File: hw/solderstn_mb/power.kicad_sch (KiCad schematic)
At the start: 74 parts, among them J301 Conn_WR-FAST_01x04, J302 Molex_MicroFit_30-43045-0421, J303 Conn_WR-FAST_01x02, Q301 Si4497DY, Q302 Si4497DY, Q303 DMG1012T, U301 TPS54332DDA, U302 TLV1117LV30DCY, U303 TLV1117LV30DCY, U304 TLV1117LV30DCY, U305 AP22811AW5

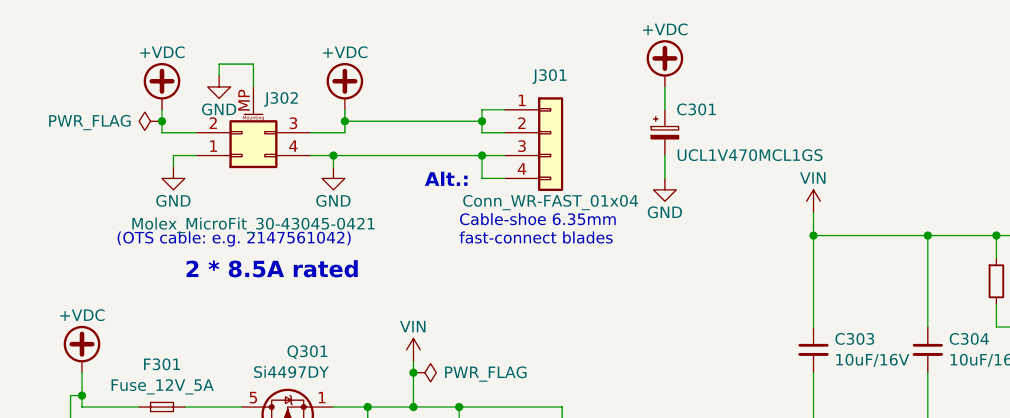
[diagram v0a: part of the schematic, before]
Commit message: Placeholder 3d-models for rear-panel (w. conns), PSU, Bottom-plate, front-panel (w. conns), outer fp
With these placeholder mech. objects, the build-in 3d view of MB pcb features most of the mechanical
objects that constrain components placements. So 3d-view can be used to quickly check and iterate
placements to avoid 3d collisions, without having to first export MB STEP into FreeCAD and muck around
only to have to repeat again for each iteration
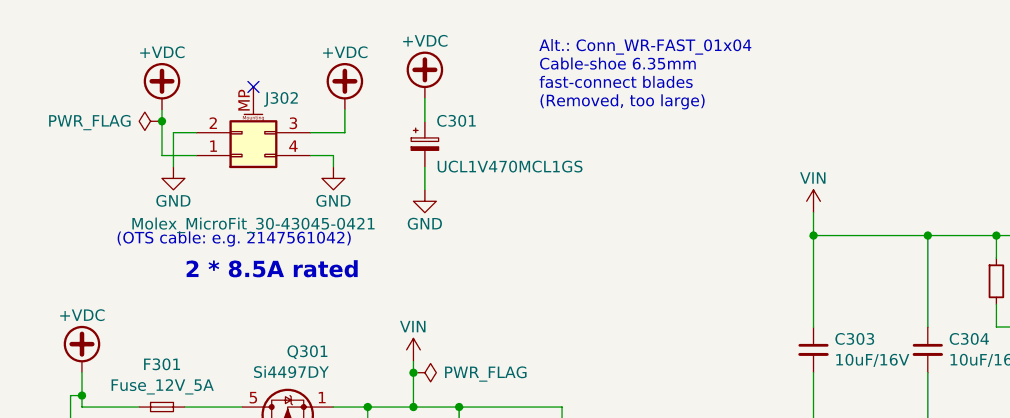
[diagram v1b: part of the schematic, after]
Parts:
- removed J301: Conn_WR-FAST_01x04, customlib_mj_fp:WR-FAST_508_4_V, symbol customlib_mj:Conn_WR-FAST_01x04
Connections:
- net +VDC: now also J302.1 (Pin_1); no longer J302.2 (Pin_2)
- net GND: now also J302.2 (Pin_2); no longer J302.1 (Pin_1), J302.MP (MountPin)
- no-connect marks 0 -> 1
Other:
- note added: "Alt.: Conn_WR-FAST_01x04 Cable-shoe 6.35mm fast-connect blades (Removed, too large)"
- note removed: "Alt.:"
- note removed: "Cable-shoe 6.35mm fast-connect blades"
- moved on the sheet: C301

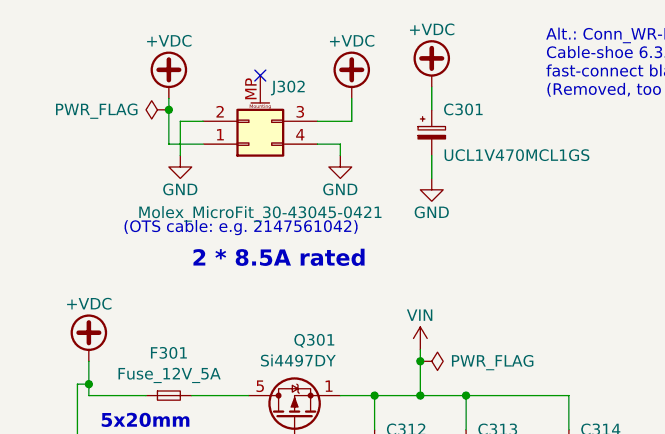
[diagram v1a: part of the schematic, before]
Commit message: solderstn_mb::power - changed generic 2x2 connector to customlib_mj:Molex_MicroFit 2x2
(and a whole bunch of other automatic changes, crap)
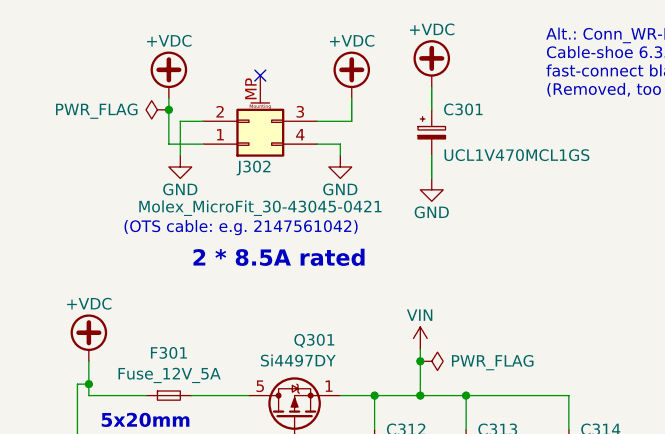
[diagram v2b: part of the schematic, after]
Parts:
- J302: symbol Connector_Generic_MountingPin:Conn_02x02_Counter_Clockwise_MountingPin -> customlib_mj:Molex_MicroFit_30-43045-0421
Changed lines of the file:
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@@
     (pin "1")
   )
-  (symbol (lib_id "Connector_Generic_MountingPin:Conn_02x02_Counter_Clockwise_MountingPin") (at 34.29 27.94 0) (mirror x) (unit 1)
+  (symbol (lib_id "customlib_mj:Molex_MicroFit_30-43045-0421") (at 34.29 27.94 0) (mirror x) (unit 1)
     (in_bom yes) (on_board yes)
-    (property "Reference" "J302" (id 0) (at 36.83 21.59 0)
+    (property "Reference" "J302" (id 0) (at 33.02 30.48 0)
       (effects (font (size 1.27 1.27)) (justify left))
     )
-    (property "Value" "Molex_MicroFit_30-43045-0421" (id 1) (at 35.56 35.56 0))
-    (property "Footprint" "customlib_mj_fp:Molex_Micro-Fit_3.0_43045-0421_2x02-1MP_P3.00mm_Horizontal" (id 2) (at 34.29 27.94 0)
+    (property "Value" "Molex_MicroFit_30-43045-0421" (id 1) (at 35.56 34.925 0))
+    (property "Footprint" "customlib_mj_fp:Molex_Micro-Fit_3.0_43045-0421_2x02-1MP_P3.00mm_Horizontal" (id 2) (at 34.29 17.78 0)
       (effects (font (size 1.27 1.27)) hide)
     )
-    (property "Datasheet" "https://www.molex.com/molex/products/part-detail/pcb_headers/0430450421" (id 3) (at 34.29 27.94 0)
+    (property "Datasheet" "https://www.molex.com/molex/products/part-detail/pcb_headers/0430450421" (id 3) (at 35.56 33.02 0)
       (effects (font (size 1.27 1.27)) hide)
     )

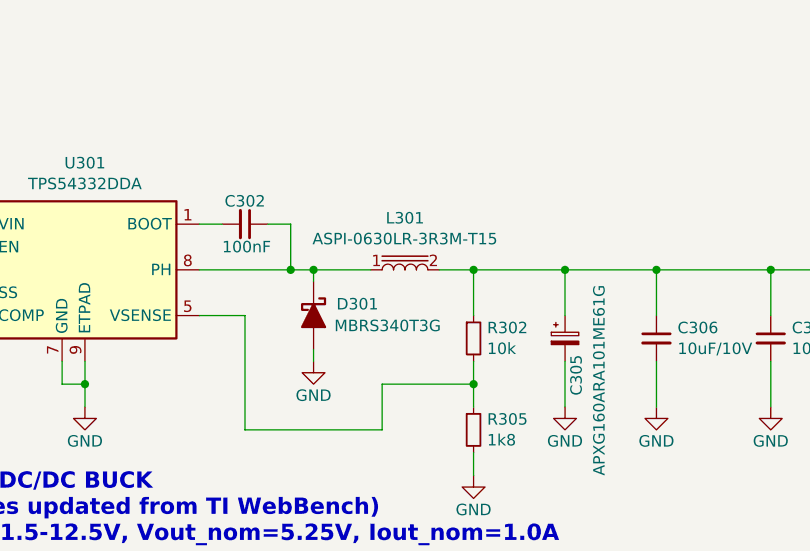
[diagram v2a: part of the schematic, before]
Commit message: hw: long-standing uncommitted stuff; mostly auto-updates (v7) fw: remove L052 tree (CMSIS & std-HAL shouldn't be committed and it was the wrong device name anyway)
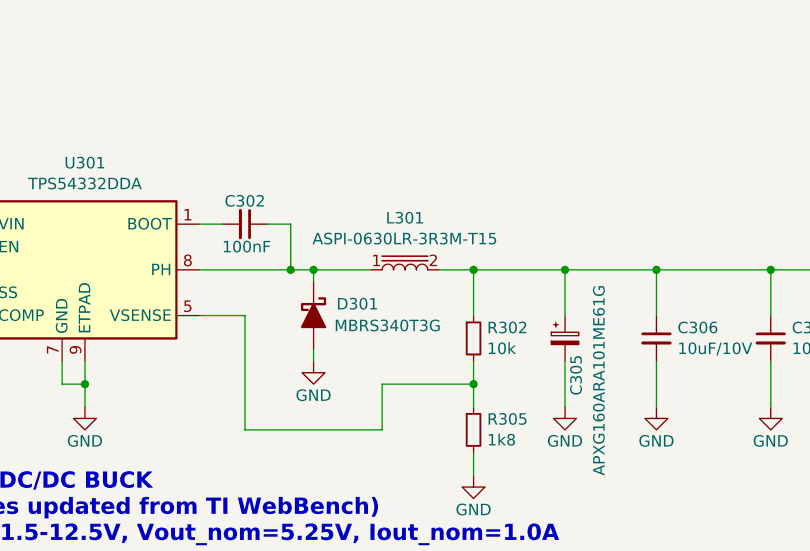
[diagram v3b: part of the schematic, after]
